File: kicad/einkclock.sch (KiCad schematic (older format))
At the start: 62 parts, among them P1 SWD, Q1 IRLIB9343PBF, Q2 IRLIB9343PBF, Q3 IRLU120N, Q4 IRLU120N, U1 MCP1702-3302ETO, U2 MC33063A, U3 MC33063A, U4 MC78L15ACP, U5 MC79L15ACP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

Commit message: Fixup schematic
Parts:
- removed L3: 10µ, Resistors_THT:R_Axial_DIN0414_L11.9mm_D4.5mm_P20.32mm_Horizontal, symbol L
- added R17: 10k, Resistors_THT:R_Axial_DIN0207_L6.3mm_D2.5mm_P10.16mm_Horizontal, symbol R
- added R18, R19: 1k, symbol R
- BT1: value 3.6-6 -> 4-6
- R15, R16: value 100k -> 10k
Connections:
- wire segments 228 -> 225
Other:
- moved on the sheet: C18, C19, U6

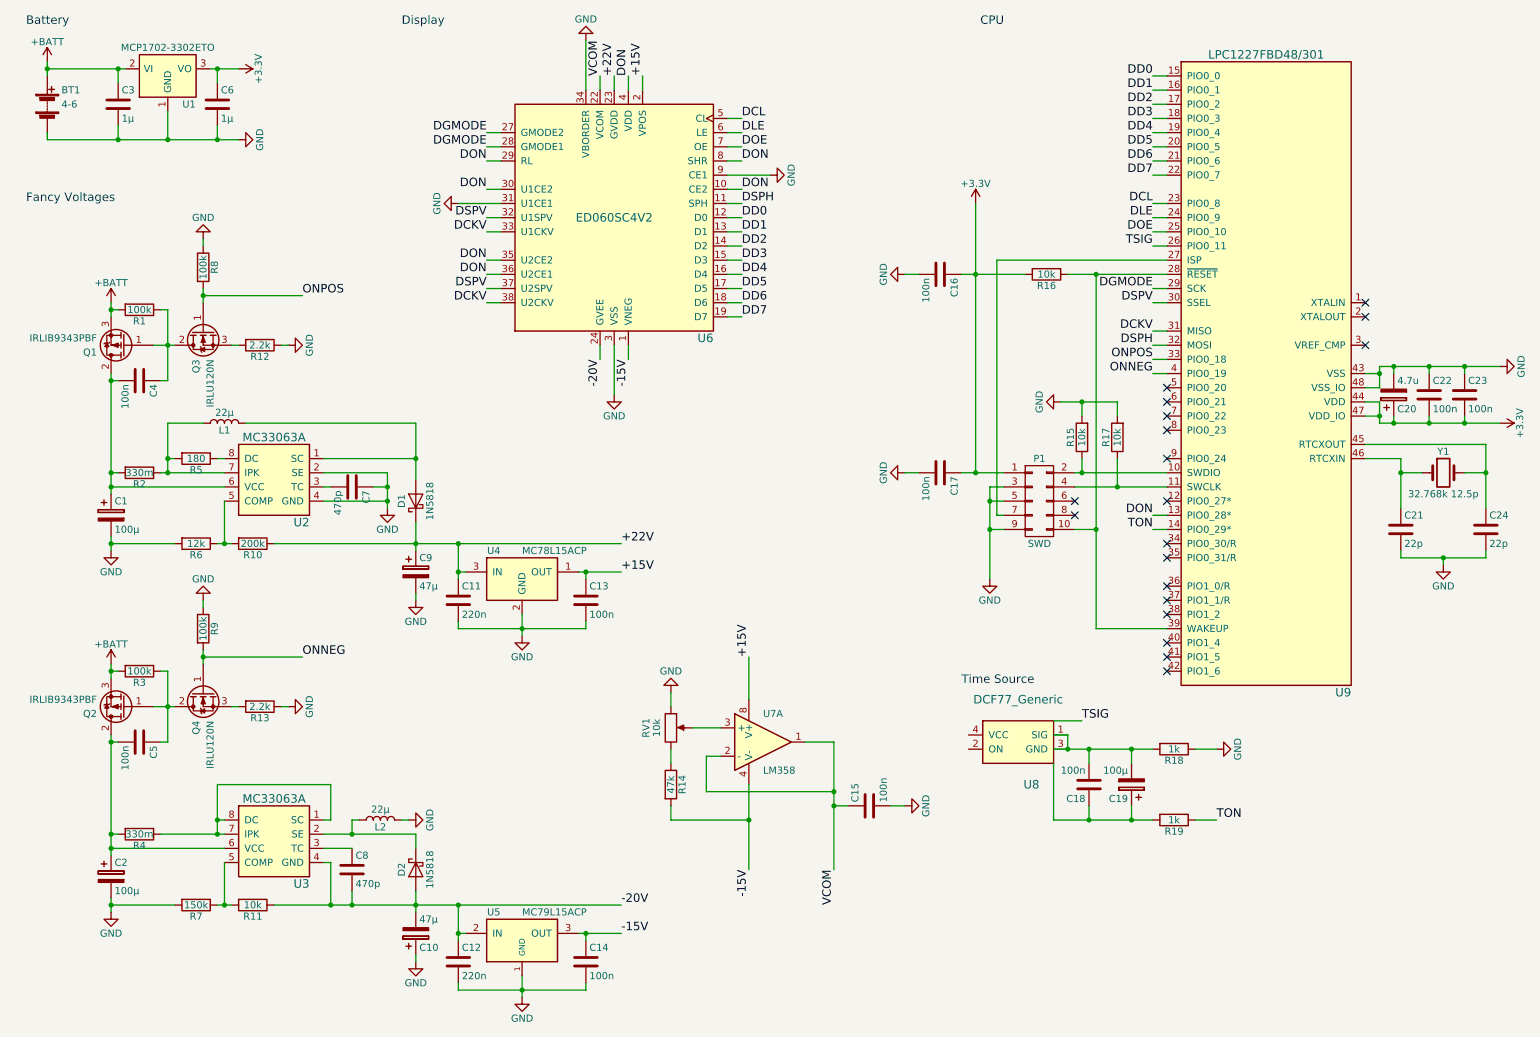
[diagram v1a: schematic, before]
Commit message: Schematic fixes
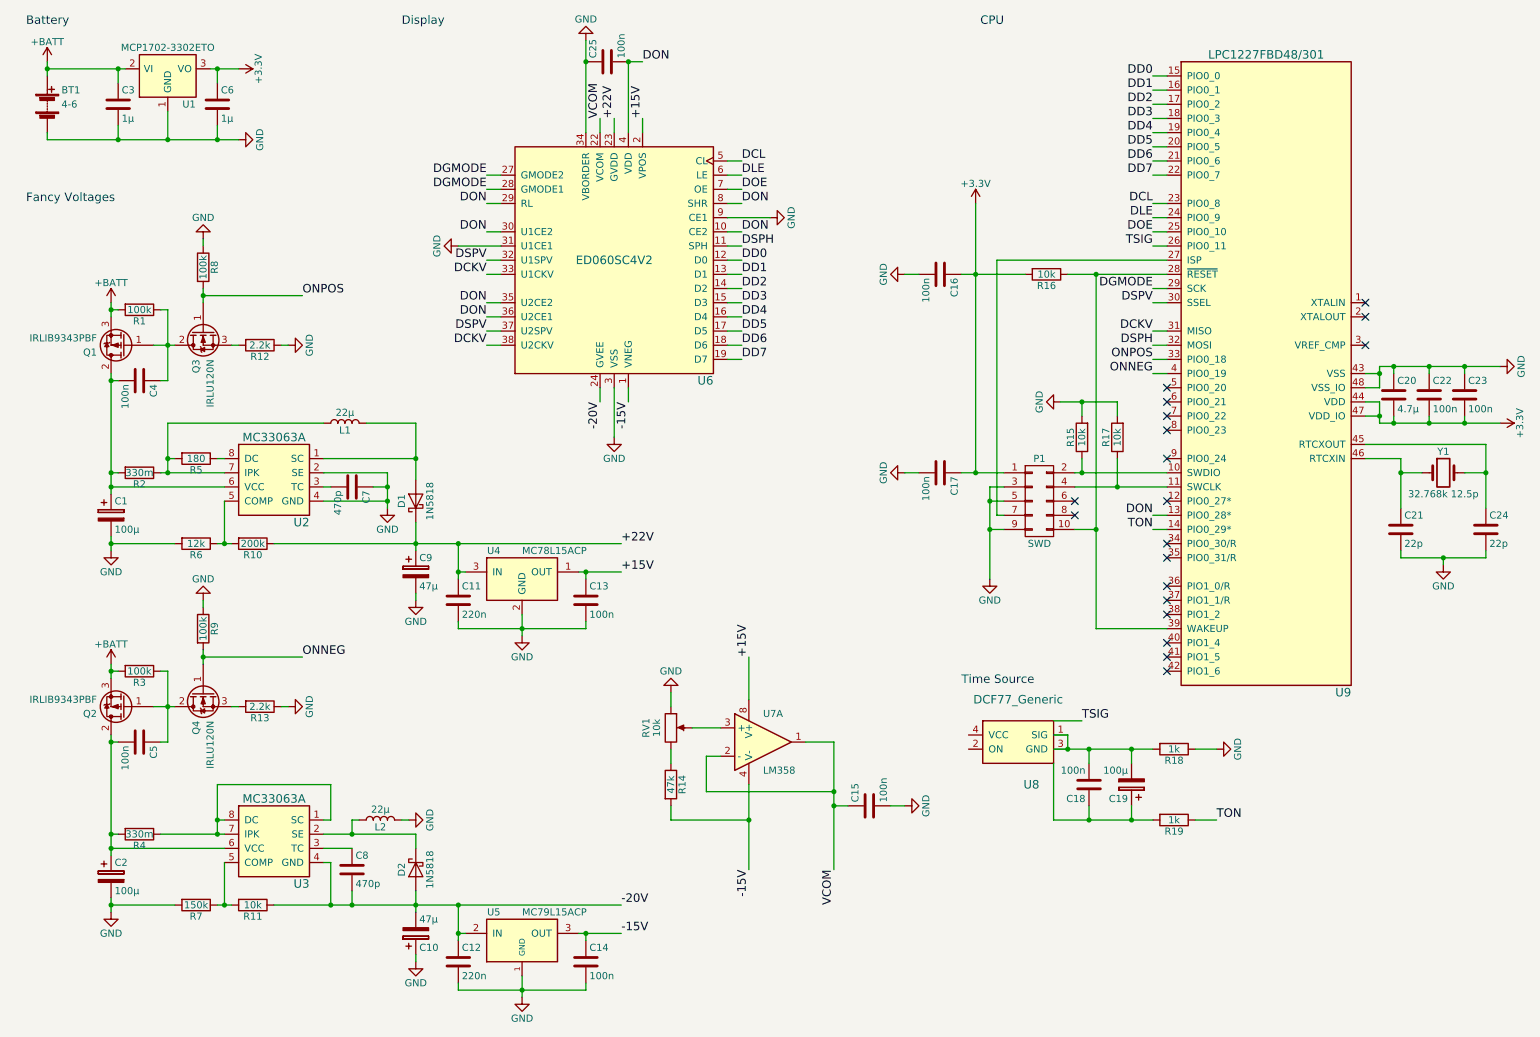
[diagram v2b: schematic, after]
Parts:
- removed C20: 4.7u, einkclock:CP_Radial_D8.0mm_P5.08mm, symbol CP
- added C20: 4.7µ, einkclock:C_Disc_D4.3mm_W1.9mm_P5.08mm, symbol C
- added C25: 100n, einkclock:C_Disc_D4.3mm_W1.9mm_P5.08mm, symbol C
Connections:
- net +3V3: now also C20.2
- net DON: now also C25.2
- net GND: now also C20.1, C25.1
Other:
- moved on the sheet: L1, U6

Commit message: Rework schematic
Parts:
- removed C1, C19, C2: 100µ, einkclock:CP_Radial_D8.0mm_P5.08mm, symbol CP
- removed C10, C9: 47µ, einkclock:CP_Radial_D10.0mm_P7.62mm, symbol CP
- removed C11, C12: 220n, einkclock:C_Disc_D4.3mm_W1.9mm_P5.08mm, symbol C
- removed C13, C14, C15, C16, C17, C18, C22, C23, C25, C4, C5: 100n, einkclock:C_Disc_D4.3mm_W1.9mm_P5.08mm, symbol C
- removed C20: 4.7µ, einkclock:C_Disc_D4.3mm_W1.9mm_P5.08mm, symbol C
- removed C21, C24: 22p, einkclock:C_Disc_D4.3mm_W1.9mm_P5.08mm, symbol C
- removed C3, C6: 1µ, einkclock:C_Disc_D4.3mm_W1.9mm_P5.08mm, symbol C
- removed C7, C8: 470p, einkclock:C_Disc_D4.3mm_W1.9mm_P5.08mm, symbol C
- removed D1, D2: 1N5818, Diodes_THT:D_DO-41_SOD81_P10.16mm_Horizontal, symbol D_Schottky
- removed L1, L2: 22µ, Resistors_THT:R_Axial_DIN0516_L15.5mm_D5.0mm_P20.32mm_Horizontal, symbol L
- removed P1: SWD, Connectors:IDC_Header_Straight_10pins, symbol CONN_02X05
- removed Q1, Q2: IRLIB9343PBF, TO_SOT_Packages_THT:TO-220_Horizontal, symbol Q_PMOS_GDS
- removed Q3, Q4: IRLU120N, TO_SOT_Packages_THT:TO-251_IPAK_Vertical, symbol Q_NMOS_GDS
- removed R1, R3, R8, R9: 100k, Resistors_THT:R_Axial_DIN0207_L6.3mm_D2.5mm_P10.16mm_Horizontal, symbol R
- removed R10: 200k, Resistors_THT:R_Axial_DIN0207_L6.3mm_D2.5mm_P10.16mm_Horizontal, symbol R
- removed R11, R15, R16, R17: 10k, Resistors_THT:R_Axial_DIN0207_L6.3mm_D2.5mm_P10.16mm_Horizontal, symbol R
- removed R12, R13: 2.2k, Resistors_THT:R_Axial_DIN0207_L6.3mm_D2.5mm_P10.16mm_Horizontal, symbol R
- removed R14: 47k, Resistors_THT:R_Axial_DIN0207_L6.3mm_D2.5mm_P10.16mm_Horizontal, symbol R
- removed R18, R19: 1k, symbol R
- removed R2, R4: 330m, Resistors_THT:R_Axial_DIN0516_L15.5mm_D5.0mm_P20.32mm_Horizontal, symbol R
- removed R5: 180, Resistors_THT:R_Axial_DIN0207_L6.3mm_D2.5mm_P10.16mm_Horizontal, symbol R
- removed R6: 12k, Resistors_THT:R_Axial_DIN0207_L6.3mm_D2.5mm_P10.16mm_Horizontal, symbol R
- removed R7: 150k, Resistors_THT:R_Axial_DIN0207_L6.3mm_D2.5mm_P10.16mm_Horizontal, symbol R
- removed RV1: 10k, einkclock:Poti_100mil_200mil, symbol POT
- removed U1: MCP1702-3302ETO, TO_SOT_Packages_THT:TO-92_Inline_Narrow_Oval, symbol MCP1703A-3302E/MB
- removed U2, U3: MC33063A, Housings_DIP:DIP-8_W7.62mm_LongPads, symbol MC33063A
- removed U4: MC78L15ACP, TO_SOT_Packages_THT:TO-92_Inline_Narrow_Oval, symbol MC78L15ACP
- removed U5: MC79L15ACP, TO_SOT_Packages_THT:TO-92_Inline_Narrow_Oval, symbol LM7905CT
- removed U6: ED060SC4V2, einkclock:Hirose_FH26-39S-0.3SHW, symbol ED060SC4V2
- removed U7: LM358, Housings_DIP:DIP-8_W7.62mm_LongPads, symbol LM358
- removed U8: DCF77_Generic, einkclock:Reichelt_DCF77_Module, symbol DCF77_Generic
- removed U9: LPC1227FBD48/301, Housings_QFP:LQFP-48_7x7mm_Pitch0.5mm, symbol LPC1227FBD48/301
- removed Y1: 32.768k 12.5p, Crystals:Crystal_AT310_d3.0mm_l10.0mm_Vertical, symbol Crystal
- BT1: value 4-6 -> 6.4-4; footprint Wire_Connections_Bridges:WireConnection_0.80mmDrill -> (none)
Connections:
- net +BATT renamed Voltage Sources/+BATT
- no-connect marks 19 -> 0
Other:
- note removed: "Battery"
- note removed: "CPU"
- note removed: "Display"
- note removed: "Fancy Voltages"
- note removed: "Time Source"

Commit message: Set most footprints
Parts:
- BT1: footprint (none) -> Wire_Connections_Bridges:WireConnection_1.00mmDrill
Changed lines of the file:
@@
 F 0 "BT1" H 1150 1750 50  0000 L CNN
 F 1 "6.4-4" H 1150 1650 50  0000 L CNN
-F 2 "" V 1050 1710 50  0001 C CNN
+F 2 "Wire_Connections_Bridges:WireConnection_1.00mmDrill" V 1050 1710 50  0001 C CNN
 F 3 "" V 1050 1710 50  0000 C CNN
 	1    1050 1650
@@
 	1050 1850 1050 1950
 $Comp
-L GND #PWR1
+L GND #PWR01
 U 1 1 58DCB02E
 P 1050 1950
-F 0 "#PWR1" H 1050 1700 50  0001 C CNN
+F 0 "#PWR01" H 1050 1700 50  0001 C CNN
 F 1 "GND" H 1050 1800 50  0000 C CNN
 F 2 "" H 1050 1950 50  0000 C CNN

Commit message: Finish BOM and fix PCB according to the parts
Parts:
- BT1: Manf# (none) -> 12BH142A-GR
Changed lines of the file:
@@
 F 2 "Wire_Connections_Bridges:WireConnection_1.00mmDrill" V 1050 1710 50  0001 C CNN
 F 3 "" V 1050 1710 50  0000 C CNN
+F 4 "12BH142A-GR" H 1050 1650 60  0001 C CNN "Manf#"
 	1    1050 1650
 	1    0    0    -1
